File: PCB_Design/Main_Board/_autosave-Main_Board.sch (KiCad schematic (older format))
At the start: 1 part

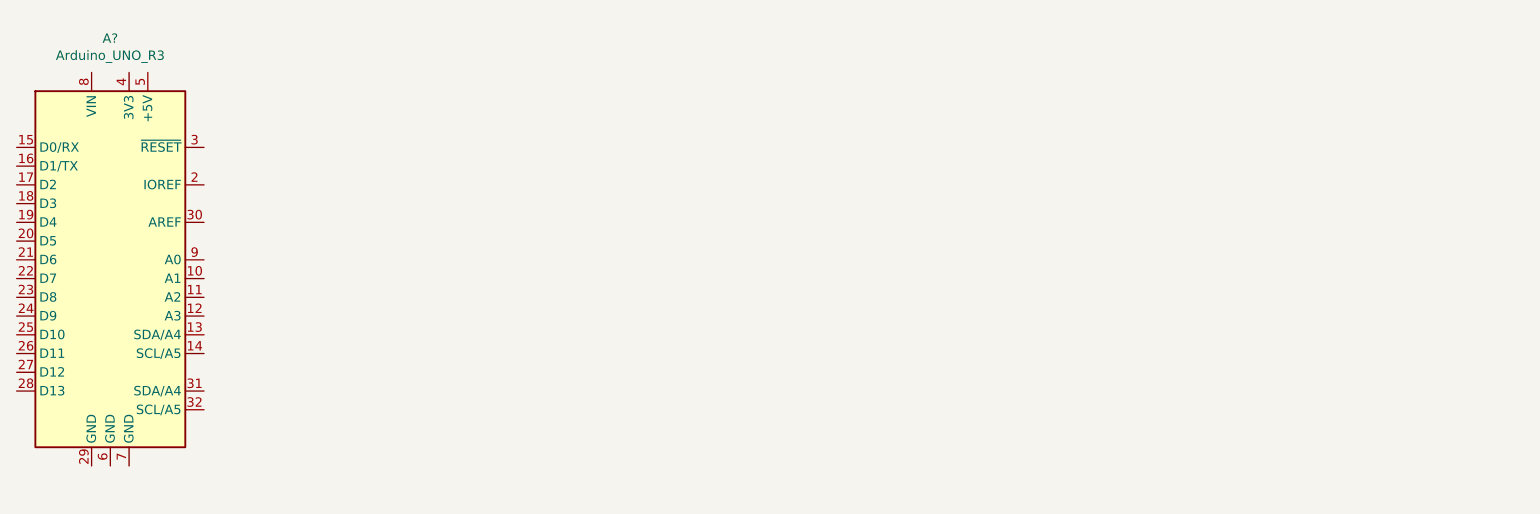
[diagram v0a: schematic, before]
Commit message: Added More Component Libraries & Footprints
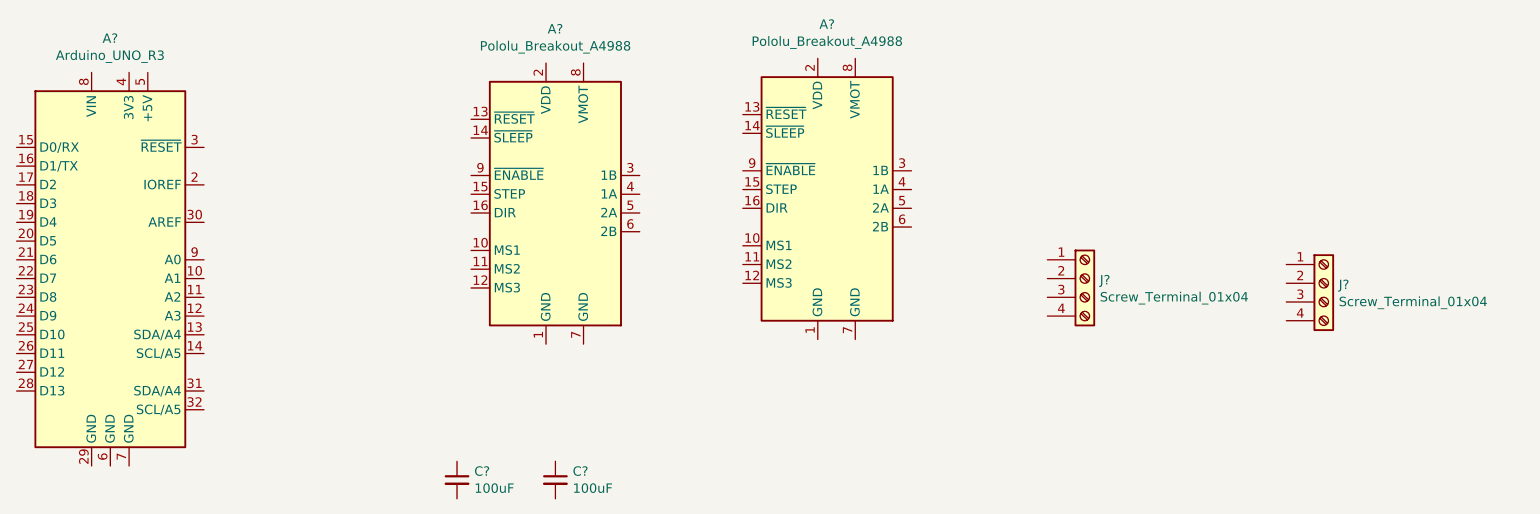
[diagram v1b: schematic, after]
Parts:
- added A? (x2): Pololu_Breakout_A4988, Module:Pololu_Breakout-16_15.2x20.3mm, symbol Driver_Motor:Pololu_Breakout_A4988
- added C? (x2): 100uF, symbol Device:C_Small
- added J? (x2): Screw_Terminal_01x04, symbol Connector:Screw_Terminal_01x04
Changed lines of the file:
@@
+	1    0    0    -1
+$EndComp
+$Comp
+L Driver_Motor:Pololu_Breakout_A4988 A?
+U 1 1 61ECC8B3
+P 5025 2875
+F 0 "A?" H 5075 3756 50  0000 C CNN
+F 1 "Pololu_Breakout_A4988" H 5075 3665 50  0000 C CNN
+F 2 "Module:Pololu_Breakout-16_15.2x20.3mm" H 5300 2125 50  0001 L CNN
+F 3 "https://www.pololu.com/product/2980/pictures" H 5125 2575 50  0001 C CNN
+	1    5025 2875
+	1    0    0    -1
+$EndComp
+$Comp
+L Driver_Motor:Pololu_Breakout_A4988 A?
+U 1 1 61ECDC3A
+P 6475 2850
+F 0 "A?" H 6525 3731 50  0000 C CNN
+F 1 "Pololu_Breakout_A4988" H 6525 3640 50  0000 C CNN
+F 2 "Module:Pololu_Breakout-16_15.2x20.3mm" H 6750 2100 50  0001 L CNN
+F 3 "https://www.pololu.com/product/2980/pictures" H 6575 2550 50  0001 C CNN
+	1    6475 2850
+	1    0    0    -1
+$EndComp
+$Comp
+L Device:C_Small C?
+U 1 1 61ECECEC
+P 4550 4400
+F 0 "C?" H 4642 4446 50  0000 L CNN
+F 1 "100uF" H 4642 4355 50  0000 L CNN
+F 2 "" H 4550 4400 50  0001 C CNN
+F 3 "~" H 4550 4400 50  0001 C CNN
+	1    4550 4400
+	1    0    0    -1
+$EndComp
+$Comp
+L Device:C_Small C?
+U 1 1 61ECFD0F
+P 5075 4400
+F 0 "C?" H 5167 4446 50  0000 L CNN
+F 1 "100uF" H 5167 4355 50  0000 L CNN
+F 2 "" H 5075 4400 50  0001 C CNN
+F 3 "~" H 5075 4400 50  0001 C CNN
+	1    5075 4400
+	1    0    0    -1
+$EndComp
+$Comp
+L Connector:Screw_Terminal_01x04 J?
+U 1 1 61ED0297
+P 7900 3325
+F 0 "J?" H 7980 3317 50  0000 L CNN
+F 1 "Screw_Terminal_01x04" H 7980 3226 50  0000 L CNN
+F 2 "" H 7900 3325 50  0001 C CNN
+F 3 "~" H 7900 3325 50  0001 C CNN
+	1    7900 3325
+	1    0    0    -1
+$EndComp
+$Comp
+L Connector:Screw_Terminal_01x04 J?
+U 1 1 61ED19AE
+P 9175 3350
+F 0 "J?" H 9255 3342 50  0000 L CNN
+F 1 "Screw_Terminal_01x04" H 9255 3251 50  0000 L CNN
+F 2 "" H 9175 3350 50  0001 C CNN
+F 3 "~" H 9175 3350 50  0001 C CNN
+	1    9175 3350
 	1    0    0    -1
 $EndComp
